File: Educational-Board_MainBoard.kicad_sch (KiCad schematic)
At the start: 0 parts

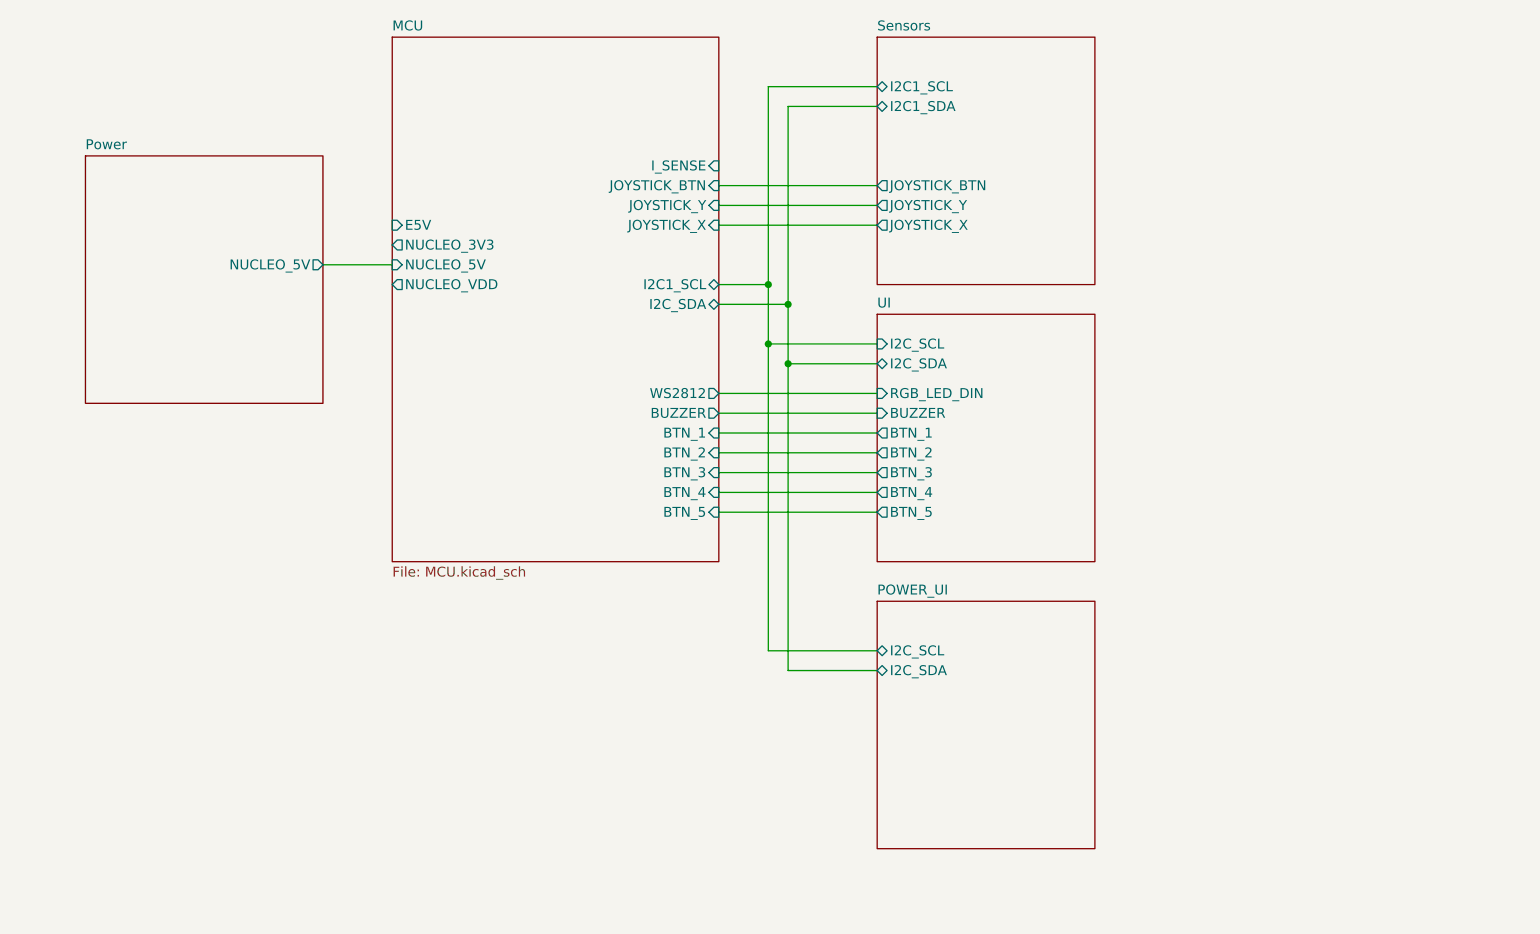
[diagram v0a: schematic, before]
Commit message: Completated the Power Schema + Added Shunts resistors with OP Amp + Connected the RGB Connector to the BUCK (Fixes #5)
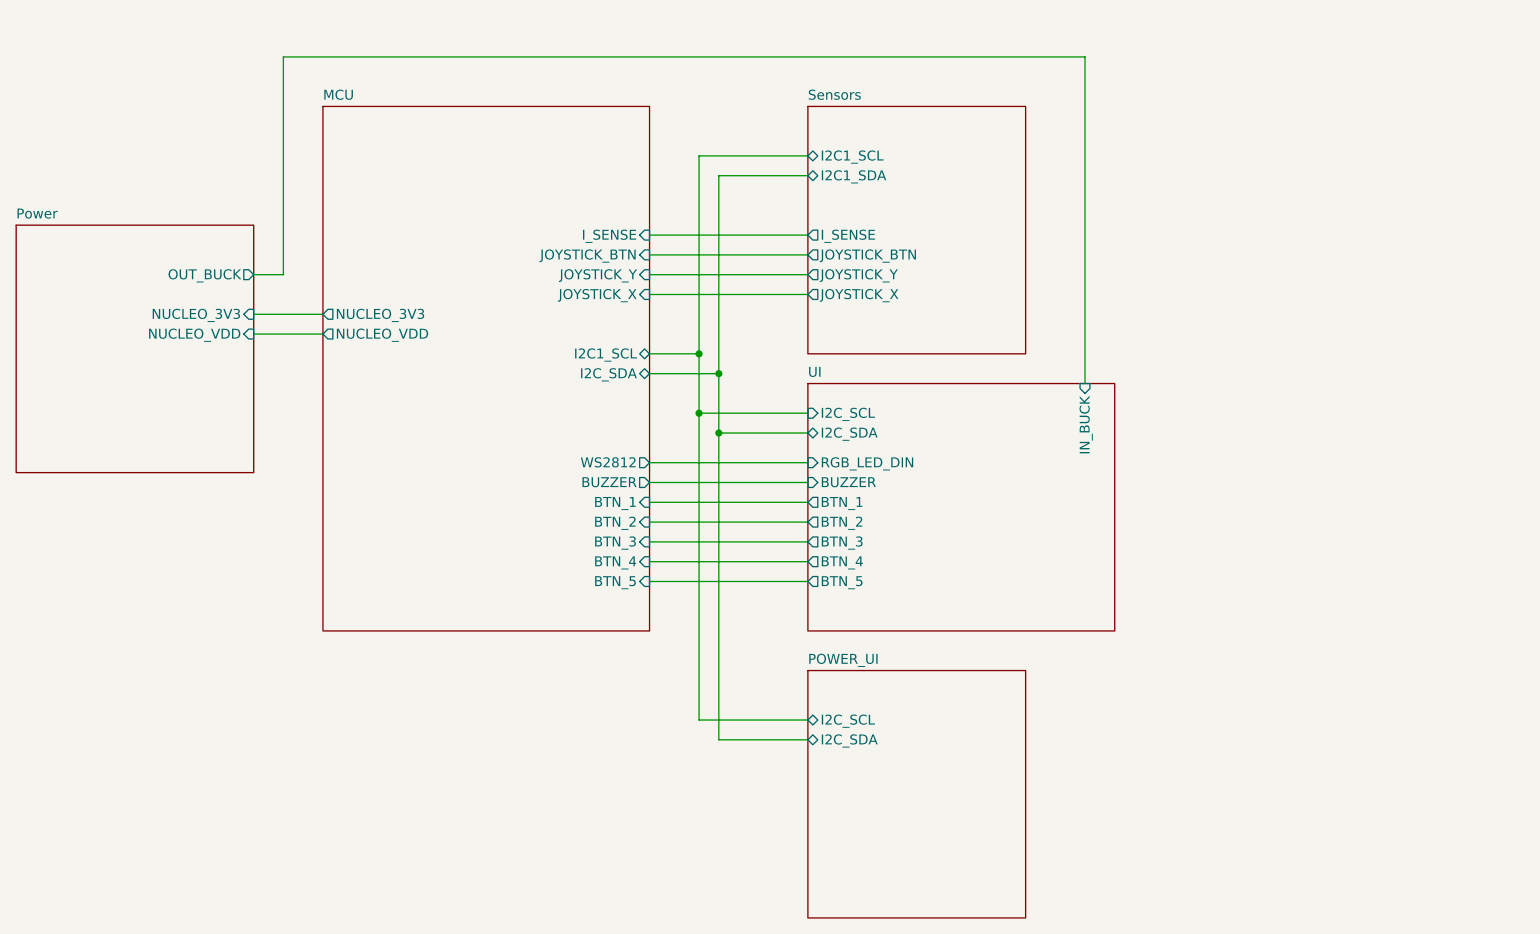
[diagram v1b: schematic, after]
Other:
- sheet MCU ports: added none; removed E5V, NUCLEO_5V
- sheet Power ports: added NUCLEO_3V3, NUCLEO_VDD, OUT_BUCK; removed NUCLEO_5V
- sheet Sensors ports: added I_SENSE; removed none
- sheet UI ports: added IN_BUCK; removed none

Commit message: Started the floorplan + added the Power LED
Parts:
- added H101, H102, H103, H104: MountingHole, MountingHole:MountingHole_3.2mm_M3_ISO14580, symbol Mechanical:MountingHole

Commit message: Continued the floor plan
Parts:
- H101, H102, H103, H104: Checked (none) -> OK
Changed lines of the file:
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@@
+			)
+		)
+		(property "Checked" "OK"
+			(at 238.76 101.6 0)
+			(effects
+				(font
+					(size 1.27 1.27)
+				)
+				(hide yes)
 			)
 		)
@@
 			)
 		)
+		(property "Checked" "OK"
+			(at 238.76 88.9 0)
+			(effects
+				(font
+					(size 1.27 1.27)
+				)
+				(hide yes)
+			)
+		)
 		(instances
 			(project "Educational-Board_MainBoard"
@@
 			)
 		)
+		(property "Checked" "OK"
+			(at 238.76 95.25 0)
+			(effects
+				(font
+					(size 1.27 1.27)
+				)
+				(hide yes)
+			)
+		)
 		(instances
 			(project "Educational-Board_MainBoard"
@@
 			(at 238.76 82.55 0)
 			(effects
+				(font
+					(size 1.27 1.27)
+				)
+				(hide yes)
+			)
+		)
+		(property "Checked" "OK"
+			(at 238.76 82.55 0)
+			(effects

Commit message: Added some netclasses + started routing of some small parts + reordered some groups
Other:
- sheet MCU ports: added I2C_SCL; removed I2C1_SCL
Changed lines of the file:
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@@
 			)
 		)
-		(pin "I2C1_SCL" bidirectional
+		(pin "I2C_SCL" bidirectional
 			(at 144.78 72.39 0)
 			(effects

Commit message: routing and silkscreen logo
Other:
- company: Filippo Castellan, Alan Masutti -> Alan Masutti, Filippo Castellan
